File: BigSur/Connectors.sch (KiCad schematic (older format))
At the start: 28 parts, among them J1 XT30, J10 XT30, J11 XT30, J12 Conn_01x04, J13 XT30, J14 XT30, J15 XT30, J16 Conn_01x03, J2 XT30, J3 XT30, J4 XT30, J5 XT30, J6 XT30, J7 XT30, J8 XT30, J9 XT30, U4 SMD42

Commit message: Cleaned up schematics
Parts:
- renumbered J16 to J11, J11 to J12, J12 to J13, J13 to J14, J14 to J15, J15 to J16
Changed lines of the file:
@@
 $EndComp
 $Comp
-L power:+24V #PWR055
+L power:+24V #PWR056
 U 1 1 5D9BEB73
 P 1250 5700
-AR Path="/5D71C3EA/5D9BEB73" Ref="#PWR055"  Part="1"
+AR Path="/5D71C3EA/5D9BEB73" Ref="#PWR056"  Part="1"
 AR Path="/5D7D29A6/5D9BEB73" Ref="#PWR?"  Part="1"
-F 0 "#PWR055" H 1250 5550 50  0001 C CNN
+F 0 "#PWR056" H 1250 5550 50  0001 C CNN
 F 1 "+24V" H 1265 5873 50  0000 C CNN
 F 2 "" H 1250 5700 50  0001 C CNN
@@
 	1400 5850 1250 5850
 $Comp
-L power:GND #PWR057
+L power:GND #PWR058
 U 1 1 5D9CDDE1
 P 1900 5900
-F 0 "#PWR057" H 1900 5650 50  0001 C CNN
+F 0 "#PWR058" H 1900 5650 50  0001 C CNN
 F 1 "GND" H 1905 5727 50  0000 C CNN
 F 2 "" H 1900 5900 50  0001 C CNN
@@
 	1400 6300 1250 6300
 $Comp
-L power:+12V #PWR059
+L power:+12V #PWR060
 U 1 1 5D9D9F04
 P 1250 6150
-F 0 "#PWR059" H 1250 6000 50  0001 C CNN
+F 0 "#PWR060" H 1250 6000 50  0001 C CNN
 F 1 "+12V" H 1265 6323 50  0000 C CNN
 F 2 "" H 1250 6150 50  0001 C CNN
@@
 GENERAL PURPOSE RELAYS
 $Comp
-L Connector_Generic:Conn_01x02 J11
+L Connector_Generic:Conn_01x02 J12
 U 1 1 5DA968D2
 P 5200 5500
-AR Path="/5D71C3EA/5DA968D2" Ref="J11"  Part="1"
+AR Path="/5D71C3EA/5DA968D2" Ref="J12"  Part="1"
 AR Path="/5D7D29A6/5DA968D2" Ref="J?"  Part="1"
-F 0 "J11" H 5280 5492 50  0000 L CNN
+F 0 "J12" H 5280 5492 50  0000 L CNN
 F 1 "XT30" H 5280 5401 50  0000 L CNN
 F 2 "" H 5200 5500 50  0001 C CNN
@@
 MOUNTING HOLES
 $Comp
-L power:GNDPWR #PWR060
+L power:GNDPWR #PWR061
 U 1 1 5DAB1B85
 P 1150 7200
-F 0 "#PWR060" H 1150 7000 50  0001 C CNN
+F 0 "#PWR061" H 1150 7000 50  0001 C CNN
 F 1 "GNDPWR" H 1154 7046 50  0000 C CNN
 F 2 "" H 1150 7150 50  0001 C CNN
@@
 	1150 7050 1150 7200
 $Comp
-L power:GNDPWR #PWR061
+L power:GNDPWR #PWR062
 U 1 1 5DABBFF8
 P 1500 7200
-F 0 "#PWR061" H 1500 7000 50  0001 C CNN
+F 0 "#PWR062" H 1500 7000 50  0001 C CNN
 F 1 "GNDPWR" H 1504 7046 50  0000 C CNN
 F 2 "" H 1500 7150 50  0001 C CNN
@@
 	1500 7050 1500 7200
 $Comp
-L power:GNDPWR #PWR062
+L power:GNDPWR #PWR063
 U 1 1 5DABF9B7
 P 1850 7200
-F 0 "#PWR062" H 1850 7000 50  0001 C CNN
+F 0 "#PWR063" H 1850 7000 50  0001 C CNN
 F 1 "GNDPWR" H 1854 7046 50  0000 C CNN
 F 2 "" H 1850 7150 50  0001 C CNN
@@
 	1850 7050 1850 7200
 $Comp
-L power:GNDPWR #PWR063
+L power:GNDPWR #PWR064
 U 1 1 5DABF9CC
 P 2200 7200
-F 0 "#PWR063" H 2200 7000 50  0001 C CNN
+F 0 "#PWR064" H 2200 7000 50  0001 C CNN
 F 1 "GNDPWR" H 2204 7046 50  0000 C CNN
 F 2 "" H 2200 7150 50  0001 C CNN
@@
 $EndComp
 $Comp
-L power:GND #PWR056
+L power:GND #PWR057
 U 1 1 5D9DB0E6
 P 8250 5750
-F 0 "#PWR056" H 8250 5500 50  0001 C CNN
+F 0 "#PWR057" H 8250 5500 50  0001 C CNN
 F 1 "GND" H 8255 5577 50  0000 C CNN
 F 2 "" H 8250 5750 50  0001 C CNN
@@
 	8250 5750 8350 5750
 $Comp
-L Connector_Generic:Conn_01x04 J12
+L Connector_Generic:Conn_01x04 J13
 U 1 1 5DA3E5B8
 P 10300 5550
-F 0 "J12" H 10380 5542 50  0000 L CNN
+F 0 "J13" H 10380 5542 50  0000 L CNN
 F 1 "Conn_01x04" H 10380 5451 50  0000 L CNN
 F 2 "" H 10300 5550 50  0001 C CNN
@@
 Connection ~ 10000 5900
 $Comp
-L power:GND #PWR058
+L power:GND #PWR059
 U 1 1 5DA8653D
 P 10000 6000
-F 0 "#PWR058" H 10000 5750 50  0001 C CNN
+F 0 "#PWR059" H 10000 5750 50  0001 C CNN
 F 1 "GND" H 10005 5827 50  0000 C CNN
 F 2 "" H 10000 6000 50  0001 C CNN
@@
 $EndComp
 $Comp
-L Connector_Generic:Conn_01x02 J13
+L Connector_Generic:Conn_01x02 J14
 U 1 1 5DAE47FD
 P 5200 5850
-AR Path="/5D71C3EA/5DAE47FD" Ref="J13"  Part="1"
+AR Path="/5D71C3EA/5DAE47FD" Ref="J14"  Part="1"
 AR Path="/5D7D29A6/5DAE47FD" Ref="J?"  Part="1"
-F 0 "J13" H 5280 5842 50  0000 L CNN
+F 0 "J14" H 5280 5842 50  0000 L CNN
 F 1 "XT30" H 5280 5751 50  0000 L CNN
 F 2 "" H 5200 5850 50  0001 C CNN
@@
 GP_RELAY_2_HIGH
 $Comp
-L Connector_Generic:Conn_01x02 J14
+L Connector_Generic:Conn_01x02 J15
 U 1 1 5DAE81B4
 P 5200 6200
-AR Path="/5D71C3EA/5DAE81B4" Ref="J14"  Part="1"
+AR Path="/5D71C3EA/5DAE81B4" Ref="J15"  Part="1"
 AR Path="/5D7D29A6/5DAE81B4" Ref="J?"  Part="1"
-F 0 "J14" H 5280 6192 50  0000 L CNN
+F 0 "J15" H 5280 6192 50  0000 L CNN
 F 1 "XT30" H 5280 6101 50  0000 L CNN
 F 2 "" H 5200 6200 50  0001 C CNN
@@
 GP_RELAY_3_HIGH
 $Comp
-L Connector_Generic:Conn_01x02 J15
+L Connector_Generic:Conn_01x02 J16
 U 1 1 5DAE81C2
 P 5200 6550
-AR Path="/5D71C3EA/5DAE81C2" Ref="J15"  Part="1"
+AR Path="/5D71C3EA/5DAE81C2" Ref="J16"  Part="1"
 AR Path="/5D7D29A6/5DAE81C2" Ref="J?"  Part="1"
-F 0 "J15" H 5280 6542 50  0000 L CNN
+F 0 "J16" H 5280 6542 50  0000 L CNN
 F 1 "XT30" H 5280 6451 50  0000 L CNN
 F 2 "" H 5200 6550 50  0001 C CNN
@@
 SOFTWARE_INVERTER_KILL
 $Comp
-L Connector_Generic:Conn_01x03 J16
+L Connector_Generic:Conn_01x03 J11
 U 1 1 5DAB1B33
 P 7300 4500
-F 0 "J16" H 7380 4542 50  0000 L CNN
+F 0 "J11" H 7380 4542 50  0000 L CNN
 F 1 "Conn_01x03" H 7380 4451 50  0000 L CNN
 F 2 "" H 7300 4500 50  0001 C CNN
@@
 	7000 4600 7000 4650
 $Comp
-L power:GND #PWR0118
+L power:GND #PWR055
 U 1 1 5DABF7D4
 P 7000 4650
-F 0 "#PWR0118" H 7000 4400 50  0001 C CNN
+F 0 "#PWR055" H 7000 4400 50  0001 C CNN
 F 1 "GND" H 7005 4477 50  0000 C CNN
 F 2 "" H 7000 4650 50  0001 C CNN

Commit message: Updated Paraduino pinout (again)
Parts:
- removed J10, J2, J3, J5, J6, J7, J8, J9: XT30, symbol Connector_Generic:Conn_01x02
- removed U4: SMD42, GeneralMCU_Example:SMD42-FTP, symbol GeneralMCU-Example:SMD42
- added J? (x8): XT30, symbol Connector_Generic:Conn_01x02
- added U?: SMD46, GeneralMCU_Example:SMD42-FTP, symbol GeneralMCU-Example:SMD46
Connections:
- net +12V: now also J4.2 (Pin_2); no longer J4.1 (Pin_1)
- net +24V: now also J1.2 (Pin_2), J?.2 (Pin_2), J?.2 (Pin_2), J?.2 (Pin_2), J?.2 (Pin_2), J?.2 (Pin_2), J?.2 (Pin_2), J?.2 (Pin_2), J?.2 (Pin_2), U?.26; no longer J1.1 (Pin_1)
- net +3V3: now also U?.3
- net +5V: now also U?.2
- net CAN_H: now also U?.19
- net CAN_L: now also U?.18
- net CAN_SHIELD: now also U?.20
- net DRV103_DUTY_CYCLE_ADJ_1: now also U?.4
- net DRV103_DUTY_CYCLE_ADJ_2: now also U?.5
- net DRV103_INPUT_1: now also U?.27
- net DRV103_INPUT_2: now also U?.28
- net DRV103_nOK: now also U?.37
- net DRV8806_RESET: now also U?.29
- net DRV8806_SERIAL_CLK: now also U?.33
- net DRV8806_SERIAL_DATIN: now also U?.32
- net DRV8806_SERIAL_DATOUT: now also U?.31
- net DRV8806_SERIAL_DATOUT_3.3V: now also U?.36
- net DRV8806_SERIAL_LATCH: now also U?.34
- net DRV8806_nENBL: now also U?.30
- net DRV8806_nFAULT: now also U?.35
- net GND: now also J1.1 (Pin_1), J11.1 (Pin_1), J4.1 (Pin_1), U?.1, U?.22, U?.25; no longer J1.2 (Pin_2), J11.3 (Pin_3), J4.2 (Pin_2)
- net GNDPWR: now also U?.21
- net GP_RELAY_1: now also U?.12
- net GP_RELAY_2: now also U?.13
- net GP_RELAY_3: now also U?.14
- net GP_RELAY_4: now also U?.15
- net PUMP_INPUT_1: now also U?.17
- net PUMP_INPUT_2: now also U?.16
- net PUMP_LS_CHANNEL_1: now also J?.1 (Pin_1)
- net PUMP_LS_CHANNEL_2: now also J?.1 (Pin_1)
- net SOFTWARE_INVERTER_KILL: now also J11.3 (Pin_3), U?.11; no longer J11.1 (Pin_1)
- net SOLENOID_CURRENT_SENSE_1: now also U?.44
- net SOLENOID_CURRENT_SENSE_2: now also U?.45
- net SOLENOID_CURRENT_SENSE_3: now also U?.46
- net SOLENOID_CURRENT_SENSE_4: now also U?.6
- net SOLENOID_ECONOMIZED_CHANNEL_1: now also J?.1 (Pin_1)
- net SOLENOID_ECONOMIZED_CHANNEL_2: now also J?.1 (Pin_1)
- net SOLENOID_ECONOMIZED_CURRENT_SENSE_1: now also U?.7
- net SOLENOID_ECONOMIZED_CURRENT_SENSE_2: now also U?.8
- net SOLENOID_LS_CHANNEL_1: now also J?.1 (Pin_1)
- net SOLENOID_LS_CHANNEL_2: now also J?.1 (Pin_1)
- net SOLENOID_LS_CHANNEL_3: now also J?.1 (Pin_1)
- net SOLENOID_LS_CHANNEL_4: now also J?.1 (Pin_1)
- no-connect marks 8 -> 10

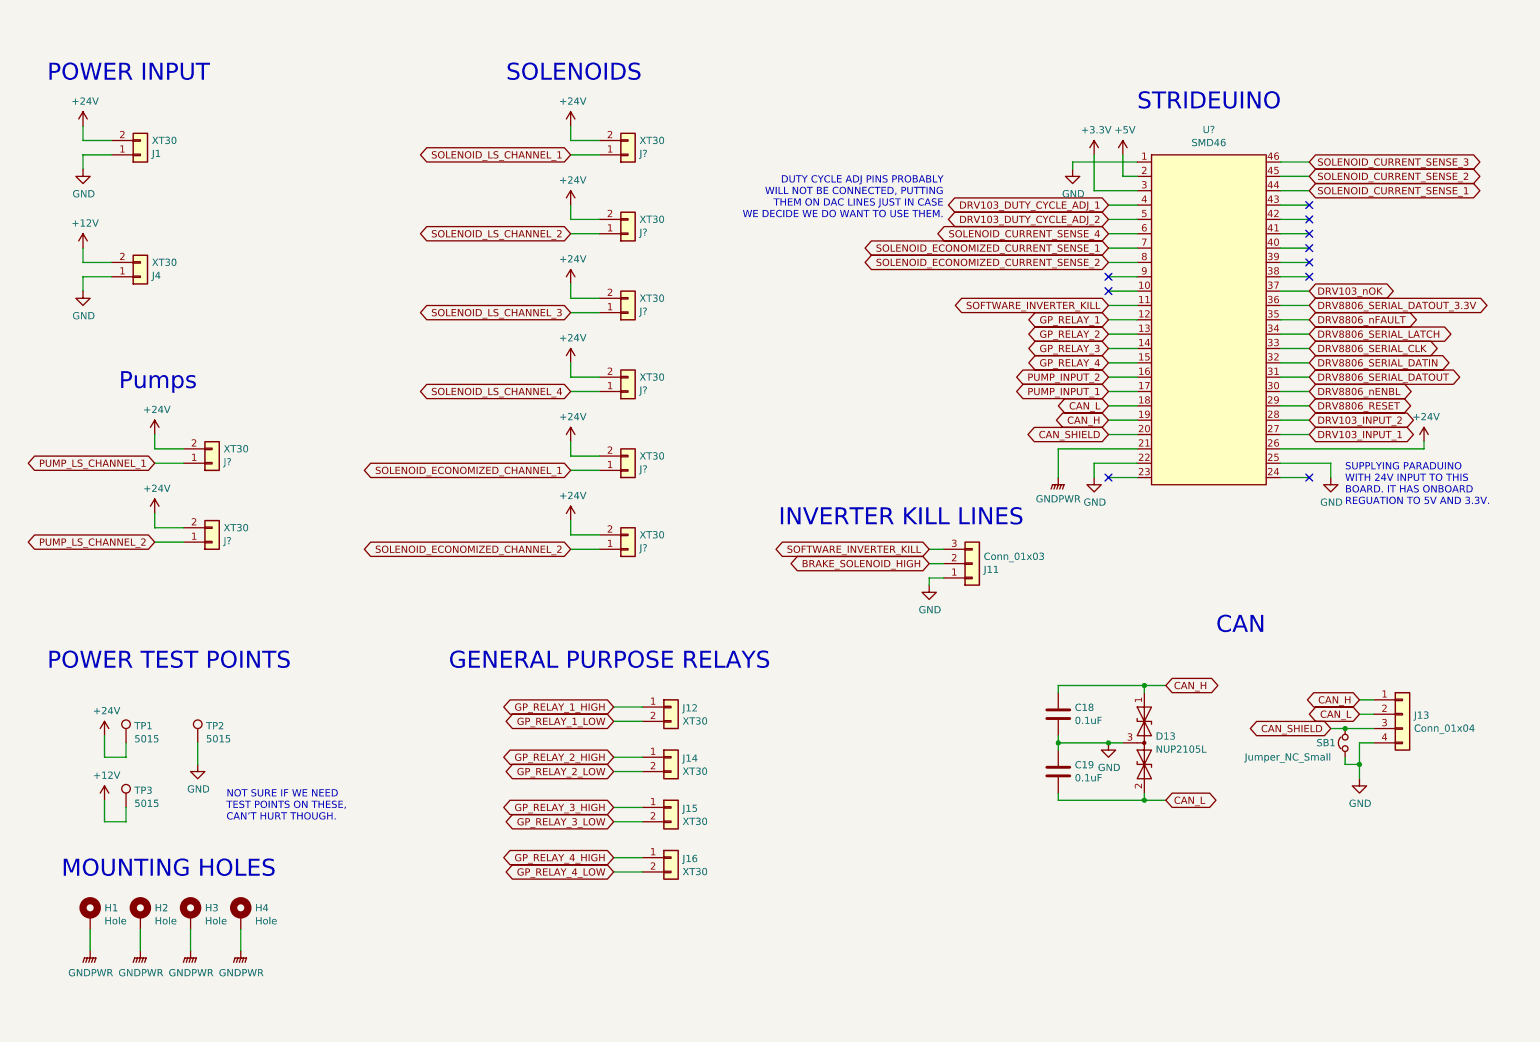
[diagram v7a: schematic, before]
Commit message: Added caps on mounting holes, reversed connector polarity
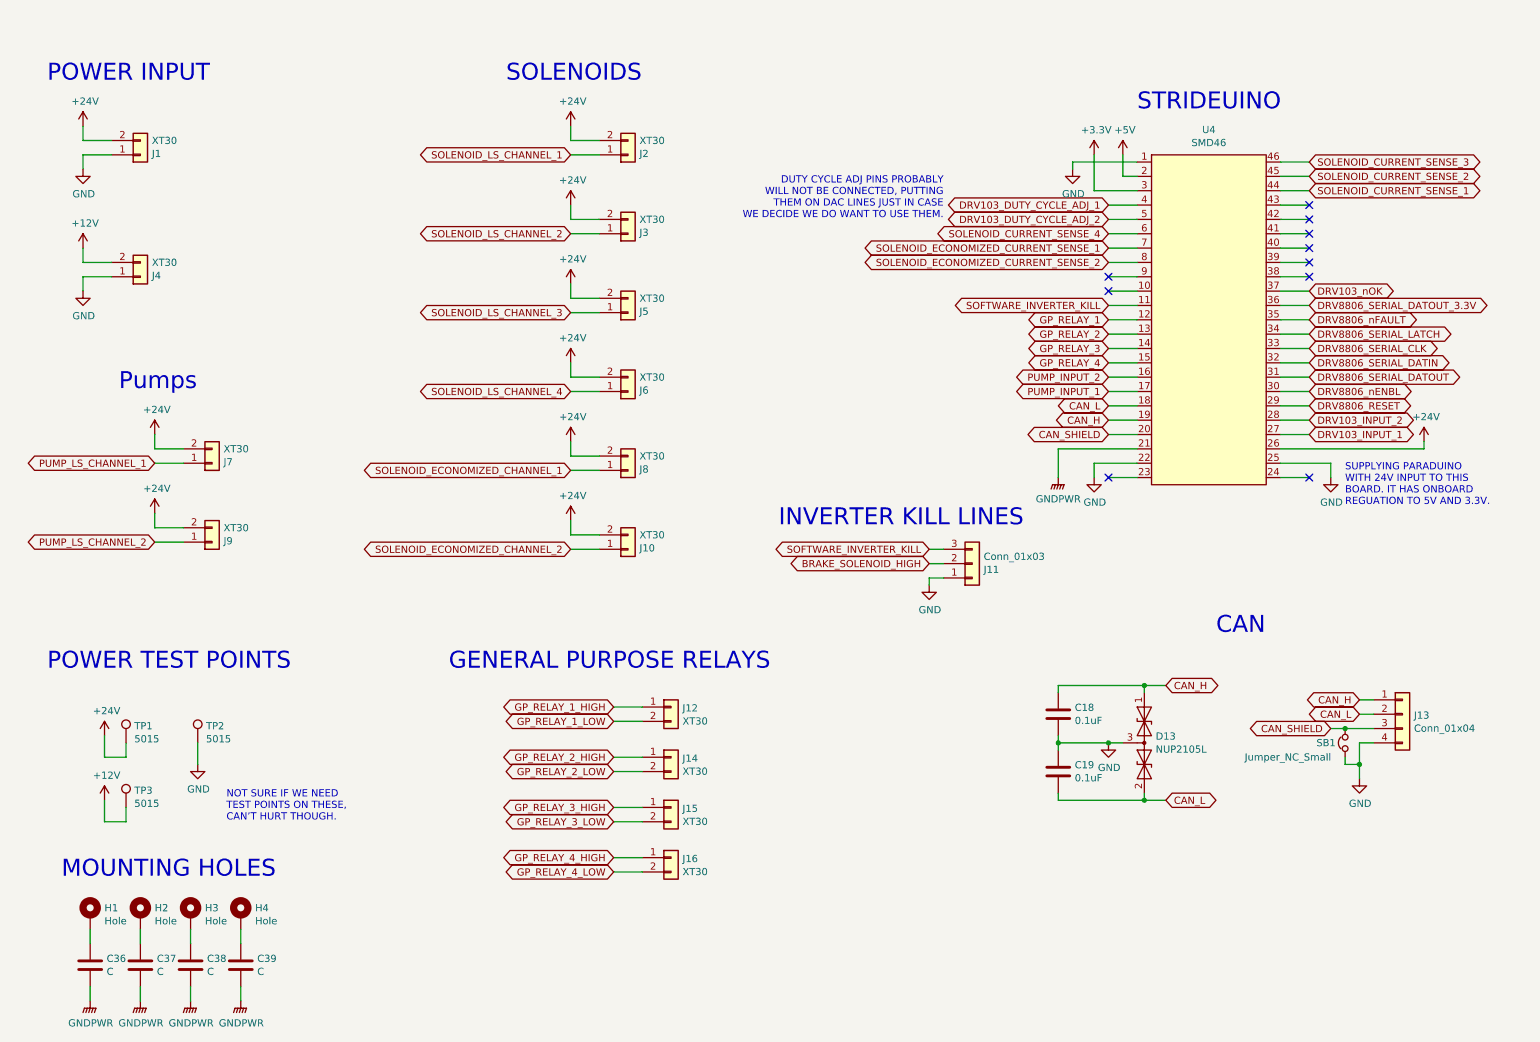
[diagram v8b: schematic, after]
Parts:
- added C36, C37, C38, C39: C, Capacitor_SMD:C_0603_1608Metric_Pad1.05x0.95mm_HandSolder, symbol Device:C
- gave numbers to parts that had none: 9
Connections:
- net GNDPWR: now also C36.2, C37.2, C38.2, C39.2; no longer H1.1, H2.1, H3.1, H4.1
- new net: C36.1, H1.1
- new net: C37.1, H2.1
- new net: C38.1, H3.1
- new net: C39.1, H4.1
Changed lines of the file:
@@
 L power:GNDPWR #PWR061
 U 1 1 5DAB1B85
-P 1150 7200
-F 0 "#PWR061" H 1150 7000 50  0001 C CNN
-F 1 "GNDPWR" H 1154 7046 50  0000 C CNN
-F 2 "" H 1150 7150 50  0001 C CNN
-F 3 "" H 1150 7150 50  0001 C CNN
-	1    1150 7200
-	1    0    0    -1
-$EndComp
-Wire Wire Line
-	1150 7050 1150 7200
+P 1150 7550
+F 0 "#PWR061" H 1150 7350 50  0001 C CNN
+F 1 "GNDPWR" H 1154 7396 50  0000 C CNN
+F 2 "" H 1150 7500 50  0001 C CNN
+F 3 "" H 1150 7500 50  0001 C CNN
+	1    1150 7550
+	1    0    0    -1
+$EndComp
+Wire Wire Line
+	1150 7050 1150 7150
 $Comp
 L power:GNDPWR #PWR062
 U 1 1 5DABBFF8
-P 1500 7200
-F 0 "#PWR062" H 1500 7000 50  0001 C CNN
-F 1 "GNDPWR" H 1504 7046 50  0000 C CNN
-F 2 "" H 1500 7150 50  0001 C CNN
-F 3 "" H 1500 7150 50  0001 C CNN
-	1    1500 7200
-	1    0    0    -1
-$EndComp
-Wire Wire Line
-	1500 7050 1500 7200
+P 1500 7550
+F 0 "#PWR062" H 1500 7350 50  0001 C CNN
+F 1 "GNDPWR" H 1504 7396 50  0000 C CNN
+F 2 "" H 1500 7500 50  0001 C CNN
+F 3 "" H 1500 7500 50  0001 C CNN
+	1    1500 7550
+	1    0    0    -1
+$EndComp
+Wire Wire Line
+	1500 7050 1500 7150
 $Comp
 L power:GNDPWR #PWR063
 U 1 1 5DABF9B7
-P 1850 7200
-F 0 "#PWR063" H 1850 7000 50  0001 C CNN
-F 1 "GNDPWR" H 1854 7046 50  0000 C CNN
-F 2 "" H 1850 7150 50  0001 C CNN
-F 3 "" H 1850 7150 50  0001 C CNN
-	1    1850 7200
-	1    0    0    -1
-$EndComp
-Wire Wire Line
-	1850 7050 1850 7200
+P 1850 7550
+F 0 "#PWR063" H 1850 7350 50  0001 C CNN
+F 1 "GNDPWR" H 1854 7396 50  0000 C CNN
+F 2 "" H 1850 7500 50  0001 C CNN
+F 3 "" H 1850 7500 50  0001 C CNN
+	1    1850 7550
+	1    0    0    -1
+$EndComp
+Wire Wire Line
+	1850 7050 1850 7150
 $Comp
 L power:GNDPWR #PWR064
 U 1 1 5DABF9CC
-P 2200 7200
-F 0 "#PWR064" H 2200 7000 50  0001 C CNN
-F 1 "GNDPWR" H 2204 7046 50  0000 C CNN
-F 2 "" H 2200 7150 50  0001 C CNN
-F 3 "" H 2200 7150 50  0001 C CNN
-	1    2200 7200
-	1    0    0    -1
-$EndComp
-Wire Wire Line
-	2200 7050 2200 7200
+P 2200 7550
+F 0 "#PWR064" H 2200 7350 50  0001 C CNN
+F 1 "GNDPWR" H 2204 7396 50  0000 C CNN
+F 2 "" H 2200 7500 50  0001 C CNN
+F 3 "" H 2200 7500 50  0001 C CNN
+	1    2200 7550
+	1    0    0    -1
+$EndComp
+Wire Wire Line
+	2200 7050 2200 7150
 $Comp
 L Device:D_TVS_x2_AAC D13
@@
 $EndComp
 $Comp
-L GeneralMCU-Example:SMD46 U?
+L GeneralMCU-Example:SMD46 U4
 U 1 1 5DAFFAE6
 P 8950 2500
-F 0 "U?" H 8950 3525 50  0000 C CNN
+F 0 "U4" H 8950 3525 50  0000 C CNN
 F 1 "SMD46" H 8950 3434 50  0000 C CNN
 F 2 "GeneralMCU_Example:SMD42-FTP" H 8950 2500 50  0001 C CNN
@@
 	8150 3800 8150 3900
 $Comp
-L power:GND #PWR?
+L power:GND #PWR0123
 U 1 1 5DB0FAD7
 P 8150 3900
-F 0 "#PWR?" H 8150 3650 50  0001 C CNN
+F 0 "#PWR0123" H 8150 3650 50  0001 C CNN
 F 1 "GND" H 8155 3727 50  0000 C CNN
 F 2 "" H 8150 3900 50  0001 C CNN
@@
 	9800 3800 9800 3900
 $Comp
-L power:GND #PWR?
+L power:GND #PWR0124
 U 1 1 5DB38914
 P 9800 3900
-F 0 "#PWR?" H 9800 3650 50  0001 C CNN
+F 0 "#PWR0124" H 9800 3650 50  0001 C CNN
 F 1 "GND" H 9805 3727 50  0000 C CNN
 F 2 "" H 9800 3900 50  0001 C CNN
@@
 $EndComp
 $Comp
-L Connector_Generic:Conn_01x02 J?
+L Connector_Generic:Conn_01x02 J10
 U 1 1 5DB64025
 P 4900 4400
-AR Path="/5D71C3EA/5DB64025" Ref="J?"  Part="1"
+AR Path="/5D71C3EA/5DB64025" Ref="J10"  Part="1"
 AR Path="/5D7D29A6/5DB64025" Ref="J?"  Part="1"
-F 0 "J?" H 4980 4392 50  0000 L CNN
+F 0 "J10" H 4980 4392 50  0000 L CNN
 F 1 "XT30" H 4980 4301 50  0000 L CNN
 F 2 "" H 4900 4400 50  0001 C CNN
@@
 $EndComp
 $Comp
-L Connector_Generic:Conn_01x02 J?
+L Connector_Generic:Conn_01x02 J8
 U 1 1 5DB644C2
 P 4900 3850
-AR Path="/5D71C3EA/5DB644C2" Ref="J?"  Part="1"
+AR Path="/5D71C3EA/5DB644C2" Ref="J8"  Part="1"
 AR Path="/5D7D29A6/5DB644C2" Ref="J?"  Part="1"
-F 0 "J?" H 4980 3842 50  0000 L CNN
+F 0 "J8" H 4980 3842 50  0000 L CNN
 F 1 "XT30" H 4980 3751 50  0000 L CNN
 F 2 "" H 4900 3850 50  0001 C CNN
@@
 $EndComp
 $Comp
-L Connector_Generic:Conn_01x02 J?
+L Connector_Generic:Conn_01x02 J6
 U 1 1 5DB64946
 P 4900 3300
-AR Path="/5D71C3EA/5DB64946" Ref="J?"  Part="1"
+AR Path="/5D71C3EA/5DB64946" Ref="J6"  Part="1"
 AR Path="/5D7D29A6/5DB64946" Ref="J?"  Part="1"
-F 0 "J?" H 4980 3292 50  0000 L CNN
+F 0 "J6" H 4980 3292 50  0000 L CNN
 F 1 "XT30" H 4980 3201 50  0000 L CNN
 F 2 "" H 4900 3300 50  0001 C CNN
@@
 $EndComp
 $Comp
-L Connector_Generic:Conn_01x02 J?
+L Connector_Generic:Conn_01x02 J5
 U 1 1 5DB64DE3
 P 4900 2750
-AR Path="/5D71C3EA/5DB64DE3" Ref="J?"  Part="1"
+AR Path="/5D71C3EA/5DB64DE3" Ref="J5"  Part="1"
 AR Path="/5D7D29A6/5DB64DE3" Ref="J?"  Part="1"
-F 0 "J?" H 4980 2742 50  0000 L CNN
+F 0 "J5" H 4980 2742 50  0000 L CNN
 F 1 "XT30" H 4980 2651 50  0000 L CNN
 F 2 "" H 4900 2750 50  0001 C CNN
@@
 $EndComp
 $Comp
-L Connector_Generic:Conn_01x02 J?
+L Connector_Generic:Conn_01x02 J3
 U 1 1 5DB65186
 P 4900 2200
-AR Path="/5D71C3EA/5DB65186" Ref="J?"  Part="1"
+AR Path="/5D71C3EA/5DB65186" Ref="J3"  Part="1"
 AR Path="/5D7D29A6/5DB65186" Ref="J?"  Part="1"
-F 0 "J?" H 4980 2192 50  0000 L CNN
+F 0 "J3" H 4980 2192 50  0000 L CNN
 F 1 "XT30" H 4980 2101 50  0000 L CNN
 F 2 "" H 4900 2200 50  0001 C CNN
@@
 $EndComp
 $Comp
-L Connector_Generic:Conn_01x02 J?
+L Connector_Generic:Conn_01x02 J2
 U 1 1 5DB655D8
 P 4900 1650
-AR Path="/5D71C3EA/5DB655D8" Ref="J?"  Part="1"
+AR Path="/5D71C3EA/5DB655D8" Ref="J2"  Part="1"
 AR Path="/5D7D29A6/5DB655D8" Ref="J?"  Part="1"
-F 0 "J?" H 4980 1642 50  0000 L CNN
+F 0 "J2" H 4980 1642 50  0000 L CNN
 F 1 "XT30" H 4980 1551 50  0000 L CNN
 F 2 "" H 4900 1650 50  0001 C CNN
@@
 $EndComp
 $Comp
-L Connector_Generic:Conn_01x02 J?
+L Connector_Generic:Conn_01x02 J9
 U 1 1 5DB6A84F
 P 2000 4350
-AR Path="/5D71C3EA/5DB6A84F" Ref="J?"  Part="1"
+AR Path="/5D71C3EA/5DB6A84F" Ref="J9"  Part="1"
 AR Path="/5D7D29A6/5DB6A84F" Ref="J?"  Part="1"
-F 0 "J?" H 2080 4342 50  0000 L CNN
+F 0 "J9" H 2080 4342 50  0000 L CNN
 F 1 "XT30" H 2080 4251 50  0000 L CNN
 F 2 "" H 2000 4350 50  0001 C CNN
@@
 $EndComp
 $Comp
-L Connector_Generic:Conn_01x02 J?
+L Connector_Generic:Conn_01x02 J7
 U 1 1 5DB6B070
 P 2000 3800
-AR Path="/5D71C3EA/5DB6B070" Ref="J?"  Part="1"
+AR Path="/5D71C3EA/5DB6B070" Ref="J7"  Part="1"
 AR Path="/5D7D29A6/5DB6B070" Ref="J?"  Part="1"
-F 0 "J?" H 2080 3792 50  0000 L CNN
+F 0 "J7" H 2080 3792 50  0000 L CNN
 F 1 "XT30" H 2080 3701 50  0000 L CNN
 F 2 "" H 2000 3800 50  0001 C CNN
@@
 	1    0    0    1
 $EndComp
+$Comp
+L Device:C C36
+U 1 1 5DB83F87
+P 1150 7300
+F 0 "C36" H 1265 7346 50  0000 L CNN
+F 1 "C" H 1265 7255 50  0000 L CNN
+F 2 "Capacitor_SMD:C_0603_1608Metric_Pad1.05x0.95mm_HandSolder" H 1188 7150 50  0001 C CNN
+F 3 "~" H 1150 7300 50  0001 C CNN
+	1    1150 7300
+	1    0    0    -1
+$EndComp
+Wire Wire Line
+	1150 7450 1150 7550
+Wire Wire Line
+	1500 7450 1500 7550
+Wire Wire Line
+	1850 7450 1850 7550
+Wire Wire Line
+	2200 7450 2200 7550
+$Comp
+L Device:C C37
+U 1 1 5DBA8313
+P 1500 7300
+F 0 "C37" H 1615 7346 50  0000 L CNN
+F 1 "C" H 1615 7255 50  0000 L CNN
+F 2 "Capacitor_SMD:C_0603_1608Metric_Pad1.05x0.95mm_HandSolder" H 1538 7150 50  0001 C CNN
+F 3 "~" H 1500 7300 50  0001 C CNN
+	1    1500 7300
+	1    0    0    -1
+$EndComp
+$Comp
+L Device:C C38
+U 1 1 5DBA8586
+P 1850 7300
+F 0 "C38" H 1965 7346 50  0000 L CNN
+F 1 "C" H 1965 7255 50  0000 L CNN
+F 2 "Capacitor_SMD:C_0603_1608Metric_Pad1.05x0.95mm_HandSolder" H 1888 7150 50  0001 C CNN
+F 3 "~" H 1850 7300 50  0001 C CNN
+	1    1850 7300
+	1    0    0    -1
+$EndComp
+$Comp
+L Device:C C39
+U 1 1 5DBA8BBF
+P 2200 7300
+F 0 "C39" H 2315 7346 50  0000 L CNN
+F 1 "C" H 2315 7255 50  0000 L CNN
+F 2 "Capacitor_SMD:C_0603_1608Metric_Pad1.05x0.95mm_HandSolder" H 2238 7150 50  0001 C CNN
+F 3 "~" H 2200 7300 50  0001 C CNN
+	1    2200 7300
+	1    0    0    -1
+$EndComp
 $EndSCHEMATC
